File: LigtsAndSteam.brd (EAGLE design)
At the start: 0 parts

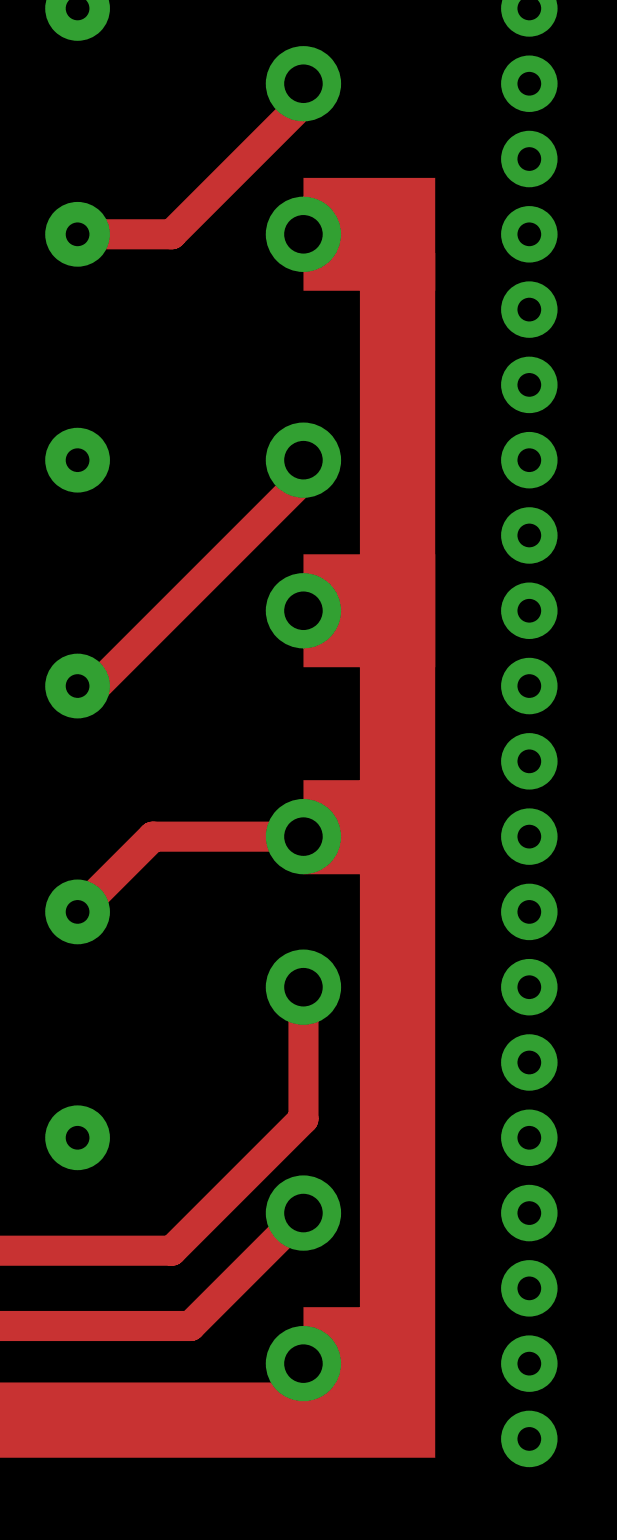
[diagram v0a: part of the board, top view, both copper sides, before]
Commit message: Added dimensions and holes
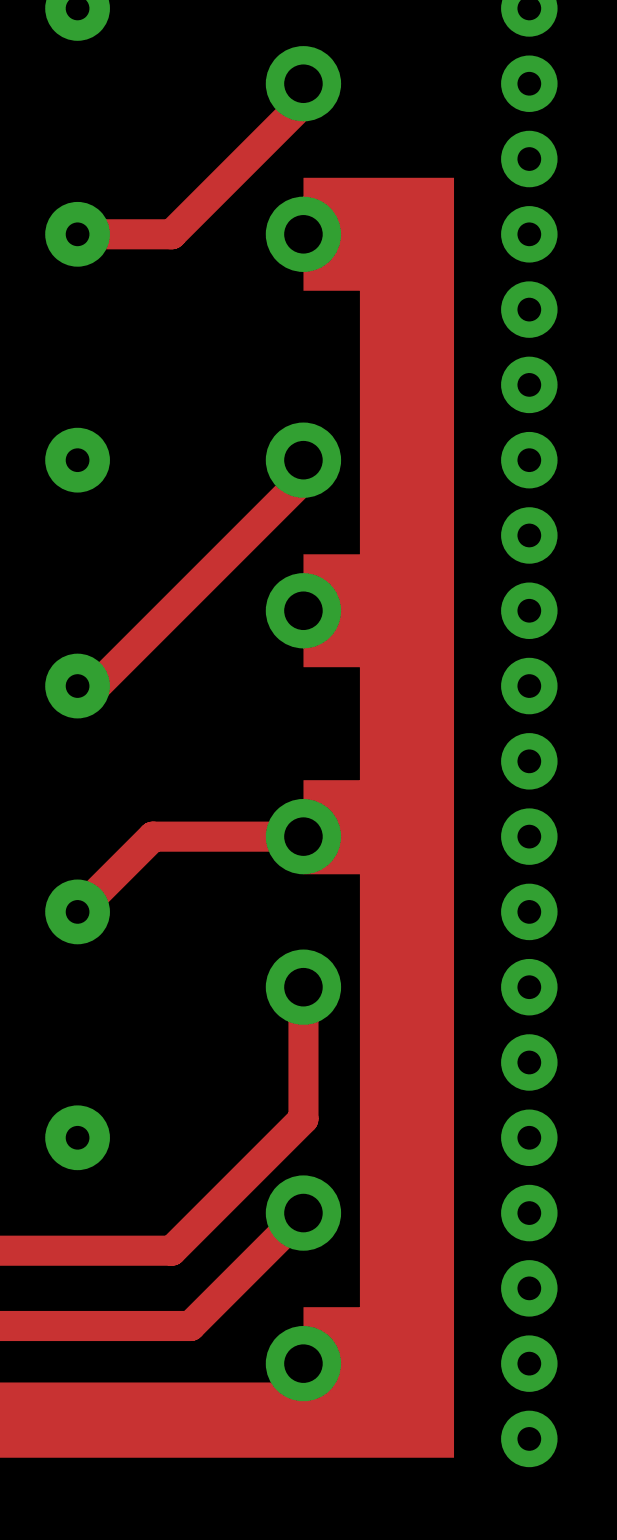
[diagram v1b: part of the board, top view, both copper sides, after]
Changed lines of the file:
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@@
 <?xml version="1.0" encoding="utf-8"?>
 <!DOCTYPE eagle SYSTEM "eagle.dtd">
-<eagle version="7.3.0">
+<eagle version="9.2.2">
 <drawing>
 <settings>
 <setting alwaysvectorfont="no"/>
+<setting keepoldvectorfont="yes"/>
 <setting verticaltext="up"/>
 </settings>
@@
 <rectangle x1="-9.525" y1="106.68" x2="-6.985" y2="109.22" layer="1"/>
 <hole x="-3.175" y="-12.065" drill="5.08"/>
+<rectangle x1="88.265" y1="-18.415" x2="88.5825" y2="24.765" layer="1"/>
+<rectangle x1="88.5825" y1="-18.415" x2="88.9" y2="24.765" layer="1"/>
+<dimension x1="89.2175" y1="109.22" x2="89.2175" y2="-18.415" x3="97.155" y3="45.4025" textsize="1.778" layer="1"/>
+<dimension x1="-9.525" y1="-18.415" x2="88.9" y2="-18.7325" x3="39.657834375" y3="-27.7698875" textsize="1.778" layer="1"/>
 </plain>
 <attributes>
@@
 <param name="dpMaxLengthDifference" value="10mm"/>
 <param name="dpGapFactor" value="2.5"/>
-<param name="checkGrid" value="0"/>
 <param name="checkAngle" value="0"/>
 <param name="checkFont" value="1"/>
 <param name="checkRestrict" value="1"/>
+<param name="checkStop" value="0"/>
+<param name="checkValues" value="0"/>
+<param name="checkNames" value="1"/>
+<param name="checkWireStubs" value="1"/>
+<param name="checkPolygonWidth" value="0"/>
 <param name="useDiameter" value="13"/>
 <param name="maxErrors" value="50"/>
@@
 </signal>
 </signals>
+<mfgpreviewcolors>
+<mfgpreviewcolor name="soldermaskcolor" color="0xC8008000"/>
+<mfgpreviewcolor name="silkscreencolor" color="0xFFFEFEFE"/>
+<mfgpreviewcolor name="backgroundcolor" color="0xFF282828"/>
+<mfgpreviewcolor name="coppercolor" color="0xFFFFBF00"/>
+<mfgpreviewcolor name="substratecolor" color="0xFF786E46"/>
+</mfgpreviewcolors>
 </board>
 </drawing>
